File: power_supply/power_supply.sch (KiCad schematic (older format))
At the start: 45 parts, among them J1 Conn_01x04_Male, J2 Conn_01x03_Male, J3 Conn_01x03_Male, J4 Conn_01x03_Male, U1 LM7815_TO220, U2 LM7915_TO220, U3 LM7805_TO220

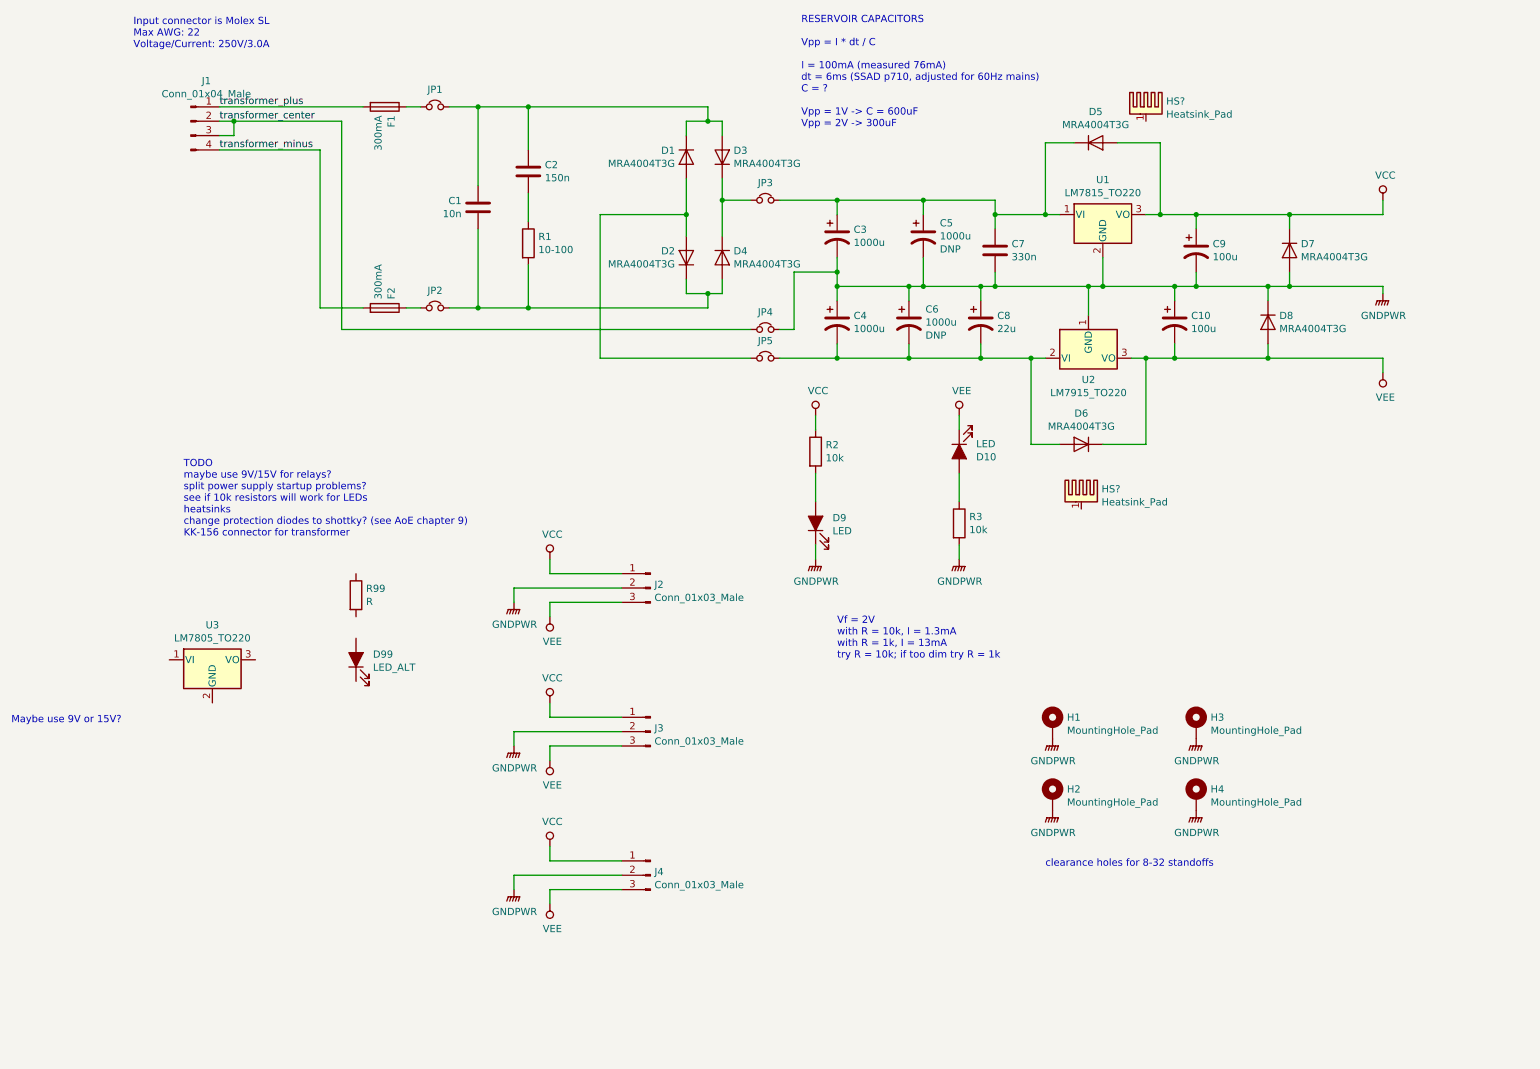
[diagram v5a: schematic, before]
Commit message: update power supply schematic to move diodes before regulators
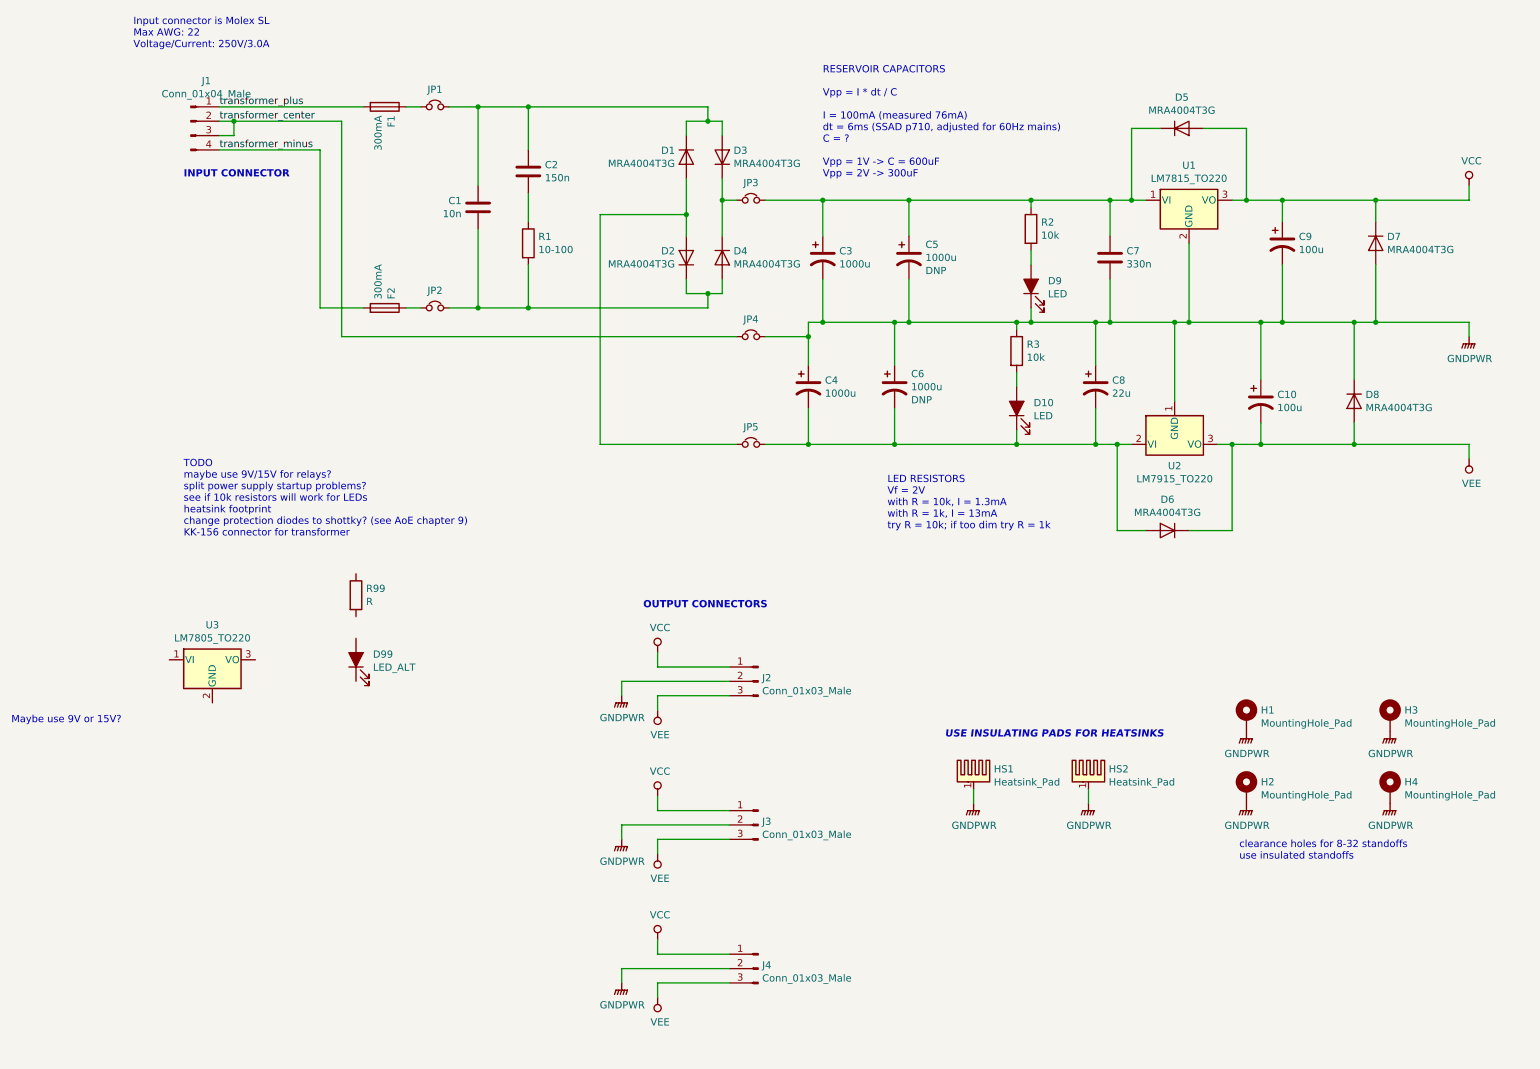
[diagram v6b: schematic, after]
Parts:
- gave numbers to parts that had none: 2
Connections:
- net GNDPWR: now also HS1.1, HS2.1, R3.1; no longer R3.2
- net VCC: no longer R2.1
- net VEE: no longer D10.1 (K)
- net at C3.1, C5.1, C7.1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: now also R2.1
- net at C4.2, C6.2, C8.2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: now also D10.1 (K)
- net at D10.2 (A): now also R3.2; no longer R3.1
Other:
- note added: "INPUT CONNECTOR"
- note added: "LED RESISTORS\nVf = 2V\nwith R = 10k, I = 1.3mA\nwith R = 1k, I = 13mA\ntry R = 10k; if too dim try R = 1k"
- note added: "OUTPUT CONNECTORS"
- note added: "TODO\nmaybe use 9V/15V for relays?\nsplit power supply startup problems?\nsee if 10k resistors will work for LEDs\nheatsink footprint\nchange protection diodes to shottky? (see AoE chapter 9)\nKK-156 connector for transformer"
- note added: "USE INSULATING PADS FOR HEATSINKS"
- note added: "clearance holes for 8-32 standoffs\nuse insulated standoffs"
- note removed: "TODO\nmaybe use 9V/15V for relays?\nsplit power supply startup problems?\nsee if 10k resistors will work for LEDs\nheatsinks\nchange protection diodes to shottky? (see AoE chapter 9)\nKK-156 connector for transformer"
- note removed: "Vf = 2V\nwith R = 10k, I = 1.3mA\nwith R = 1k, I = 13mA\ntry R = 10k; if too dim try R = 1k"
- note removed: "clearance holes for 8-32 standoffs"
- moved on the sheet: C10, C3, C4, C5, C6, C7, C8, C9, D10, D5, D6, D7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
